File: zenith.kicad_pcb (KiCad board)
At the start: 2 copper layers, 38.1 x 40.3 mm, 79 parts, among them J1 Screw_Terminal_01x02, J2 Conn_01x03, J3 Conn_01x03, SW1 TS-1088-AR02016, SW2 TS-1088-AR02016, U1 TPS63070RNMR, U2 BMP580, U3 BQ25883RGER, U4 ICM-45686, U5 STM32F722RETx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

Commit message: finished pcb
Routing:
- net GND: track 0.00 -> 126.9 mm, vias 0 -> 22
- net /BQ_INT: track 6.20 -> 86.2 mm, vias 0 -> 2
- net /I2C_SCL: track 16.7 -> 77.1 mm, vias 4 -> 6
- net /I2C_SDA: track 13.1 -> 62.5 mm, vias 2 -> 4
- net /SD_CD: track 0.00 -> 32.7 mm, vias 0 -> 2
- net /SD_CLK: track 0.00 -> 26.8 mm, vias 0 -> 2
- net /SD_CMD: track 0.00 -> 23.2 mm, vias 0 -> 2
- net /SD_DAT3: track 1.32 -> 23.8 mm, vias 0 -> 2
- net VSYS: track 75.1 -> 95.6 mm, vias 4 -> 6
- net /SD_DAT1: track 1.76 -> 19.3 mm, vias 0 -> 2
- net /SD_DAT0: track 1.57 -> 17.6 mm, vias 0 -> 2
- net /SD_DAT2: track 1.48 -> 16.5 mm, vias 0 -> 2
- net /ICM_SCK: track 0.00 -> 11.6 mm, vias 0 -> 2
- net /ICM_SDI: track 0.00 -> 9.88 mm, vias 0 -> 2
- net +3.3V: track 147.1 -> 154.5 mm
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- added copper zone on B.Cu, net GND
- added copper zone on F.Cu, net GND
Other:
- board size 38.1 x 40.3 mm -> 38.3 x 41.4 mm

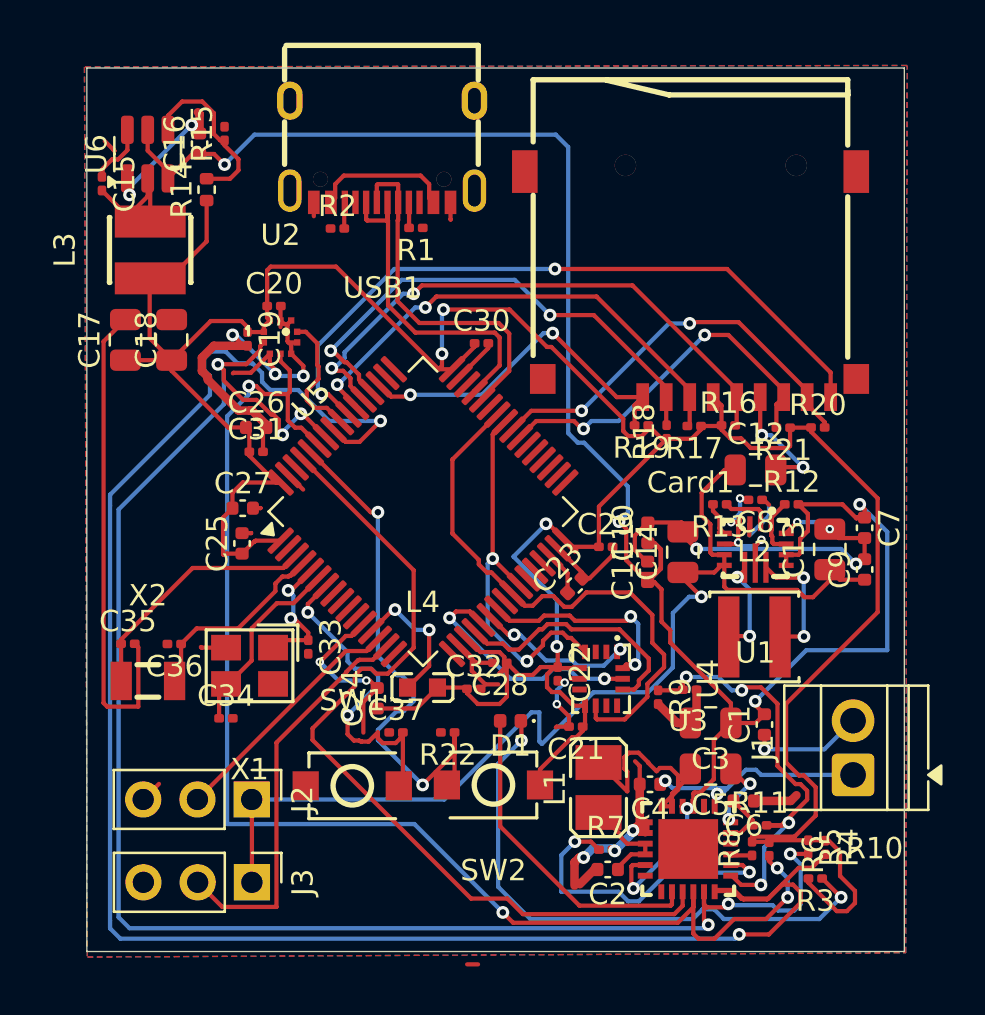
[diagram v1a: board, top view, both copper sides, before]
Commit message: added LEDs, finished pcb
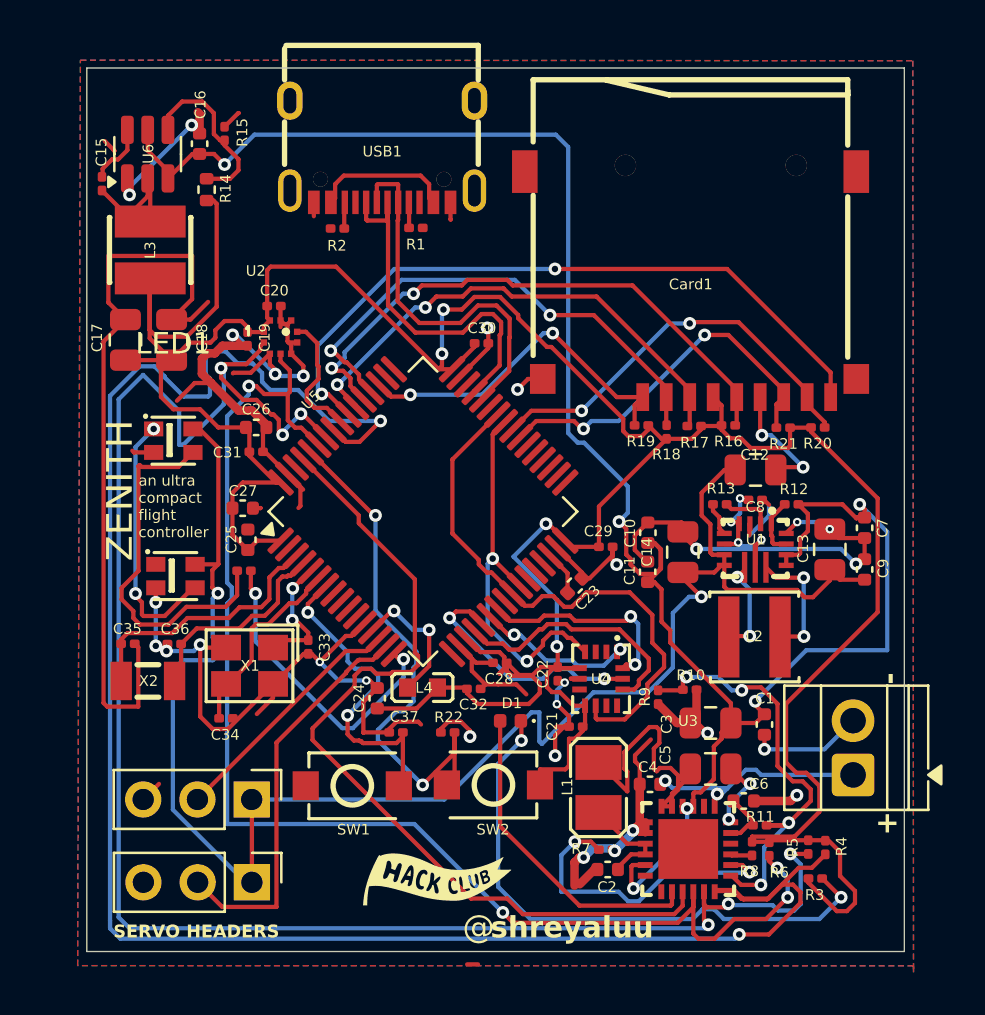
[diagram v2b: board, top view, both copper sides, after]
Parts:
- added LED1: WS2812B-2020, lcsc:LED-SMD_4P-L2.0-W2.0-TL_WS2812B-2020, F.Cu at (105.5, 81.2)
- added LED2: WS2812B-2020, lcsc:LED-SMD_4P-L2.0-W2.0-TL_WS2812B-2020, F.Cu at (105.6, 87.5)
- added R23: 330, Resistor_SMD:R_0201_0603Metric, F.Cu at (108.8, 87.3)
- SERVO HEADERS: renamed from J3
- moved C25 0.32 mm to (109.0, 85.8)
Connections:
- U5 pad 16: unconnected-(U5-PA2-Pad16) -> /LED_DIN
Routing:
- net GND: track 126.9 -> 177.9 mm, vias 22 -> 33
- net +5V: track 50.9 -> 77.6 mm, vias 1 -> 2
- net Net-(LED1-DI): track 0.00 -> 17.4 mm
- net /LED_DIN: track 0.00 -> 14.4 mm, vias 0 -> 2
- net Net-(LED1-DO): track 0.00 -> 12.2 mm, vias 0 -> 2
- net +3.3V: track 154.5 -> 165.4 mm
- net /I2C_SCL: track 77.1 -> 83.2 mm
- net /BQ_INT: track 86.2 -> 90.0 mm
- net /BTST: track 11.1 -> 13.7 mm
- net /USB_DP: track 16.4 -> 17.6 mm
- net /USB_DN: track 16.8 -> 17.9 mm
- net /LSE_IN: track 11.7 -> 12.5 mm
- net /BQ_CE: track 39.8 -> 40.6 mm
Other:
- board text added: "+"
- board text added: "-"
- board text added: "@"
- board text added: "ZENITH"
- board text added: "an ultra compact flight controller"
- board text added: "shreyaluu"
